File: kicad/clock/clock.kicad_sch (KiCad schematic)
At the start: 6 parts

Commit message: Working on clock
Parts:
- removed U5: ~, Package_DIP:DIP-14_W7.62mm, symbol custom_symbol_lib:quad_and
- removed U6: ~, Package_DIP:DIP-14_W7.62mm, symbol custom_symbol_lib:6xNOT
- removed U7: ~, Package_DIP:DIP-14_W7.62mm, symbol custom_symbol_lib:quad_OR
- added C1: C, Capacitor_THT:C_Disc_D5.0mm_W2.5mm_P5.00mm, symbol Device:C
- added R2, R3, R4, R5: R, custom_footprint_library:0.4_pitch_resistor, symbol Device:R
- added U4: ~, Package_DIP:DIP-14_W7.62mm, symbol custom_symbol_lib:OP_AMP_quad
- U1: footprint custom_footprint_library:bus_connector -> Connector_PinHeader_2.54mm:PinHeader_1x23_P2.54mm_Vertical
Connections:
- net at U2.7 (Q7), U3.7 (Q7): now also U1.14 (D0); no longer U1.12 (D0)
- net at U2.6 (Q6), U3.6 (Q6): now also U1.15 (D1); no longer U1.13 (D1)
- net at U2.5 (Q5), U3.5 (Q5): now also U1.16 (D2); no longer U1.14 (D2)
- net at U2.4 (Q4), U3.4 (Q4): now also U1.17 (D3); no longer U1.15 (D3)
- net at U2.3 (Q3), U3.3 (Q3): now also U1.18 (D4); no longer U1.16 (D4)
- net at U2.2 (Q2), U3.2 (Q2): now also U1.19 (D5); no longer U1.17 (D5)
- net at U2.1 (Q1), U3.1 (Q1): now also U1.20 (D6); no longer U1.18 (D6)
- net at U2.15 (Q0), U3.15 (Q0): now also U1.21 (D7); no longer U1.19 (D7)
- net at U3.11 (CCLK): now also U2.9 (RCO#); no longer U2.11 (CCLK)
- net at U3.12 (CCKEN#): now also U2.12 (CCKEN#), U2.8 (GND); no longer U2.9 (RCO#)
- new net: R2.1, U4.4 (V+)
- new net: R2.2, R3.1, R5.2, U4.3 (IN+_1)
- new net: C1.1, R4.2, U4.2 (IN-_1)
- new net: C1.2, R3.2, U4.10 (IN+_3), U4.11 (GND), U4.12 (IN+_4), U4.13 (IN-_4), U4.5 (IN+_2), U4.6 (IN-_2), U4.9 (IN-_3)
- new net: R4.1, R5.1, U4.1 (OUT_1)
- no-connect marks 4 -> 9
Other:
- note added: "Counter A"
- note added: "Counter B"
- note removed: "A & B CLK generator"
- note removed: "Auto clock source"
- note removed: "Manual / auto clock selector"

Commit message: Working on clock
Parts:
- added R1, R6, R7, R8: R, custom_footprint_library:0.4_pitch_resistor, symbol Device:R
- added U10, U14, U17, U5: ~, Package_DIP:DIP-14_W7.62mm, symbol custom_symbol_lib:quad_and
- added U11: ~, Package_DIP:DIP-14_W7.62mm, symbol custom_symbol_lib:dual_latch
- added U12, U15, U16, U18, U20, U21: ~, custom_footprint_library:jumper, symbol custom_symbol_lib:jumper
- added U13, U6: ~, Package_DIP:DIP-14_W7.62mm, symbol custom_symbol_lib:6xNOT
- added U19: ~, Package_DIP:DIP-16_W7.62mm, symbol custom_symbol_lib:8_bit_counter
- added U7, U8: ~, Connector_PinHeader_2.54mm:PinHeader_1x03_P2.54mm_Vertical, symbol custom_symbol_lib:switch_SPDT
- added U9: ~, Package_DIP:DIP-14_W7.62mm, symbol custom_symbol_lib:quad_OR
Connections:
- net at R2.1, U4.4 (V+): now also U1.12 (V+), U2.10 (CCLR#), U2.16 (V+), U3.10 (CCLR#), U3.16 (V+), R1.1, R6.1, U10.14 (V+), U11.14 (V+), U13.14 (V+), U14.14 (V+), U17.14 (V+), U19.10 (CCLR#), U19.16 (V+), U5.14 (V+), U6.14 (V+), U9.14 (V+)
- net at C1.2, R3.2, U4.10 (IN+_3)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: now also U1.13 (GND), U2.12 (CCKEN#), U2.8 (GND), U3.12 (CCKEN#), U3.8 (GND), U10.7 (GND), U11.10 (1RESET), U11.4 (0RESET), U11.6 (0SET), U11.7 (GND), U11.8 (1SET), U12.2 (GND), U13.7 (GND), U14.7 (GND), U15.2 (GND), U16.2 (GND), U17.12 (3B), U17.13 (3A), U17.4 (2A), U17.5 (2B), U17.7 (GND), U18.2 (GND), U19.12 (CCKEN#), U19.14 (OE#), U19.8 (GND), U20.2 (GND), U21.2 (GND), U5.7 (GND), U6.13 (I5), U6.7 (GND), U7.2 (2_(middle)), U8.2 (2_(middle)), U9.5 (1A), U9.6 (1B), U9.7 (GND)
- net at R4.1, R5.1, U4.1 (OUT_1): now also U12.1 (IN)
- net at U1.10 (CLK_A): now also U21.3 (OUT)
- net at U1.11 (CLK_B): now also U11.11 (1CLK), U11.3 (0CLK), U20.3 (OUT)
- net at U1.22 (FAULT): now also U17.2 (1B)
- net at U1.23 (ENABLE): now also U10.10 (4A), U10.12 (3B)
- net at U1.5 (WRITE_0): now also U10.1 (1A)
- net at U1.6 (WRITE_1): now also U10.4 (2A)
- net at U1.9 (READ_READY): now also U9.11 (Q3)
- net at U3.13 (RCLK): now also U10.8 (4Q), U13.5 (I2), U9.13 (3B)
- net at U3.14 (OE#): now also U13.6 (O2)
- net at U2.11 (CCLK): now also U18.3 (OUT), U19.11 (CCLK), U19.13 (RCLK)
- net at U2.13 (RCLK): now also U10.11 (3Q), U13.9 (I3), U9.12 (3A)
- net at U2.14 (OE#): now also U13.8 (03)
- new net: R1.2, U5.1 (1A), U7.1
- new net: R6.2, U5.4 (2A), U7.3
- new net: U17.9 (4B), U19.1 (Q1), U9.9 (2B)
- new net: U13.11 (I4), U19.15 (Q0), U9.8 (2A)
- new net: U12.3 (OUT), U14.12 (3B)
- new net: U20.1 (IN), U6.10 (O4)
- new net: U16.1 (IN), U5.5 (2B), U6.4 (O1)
- new net: U14.9 (4B), U16.3 (OUT)
- new net: U14.11 (3Q), U9.1 (0A)
- new net: U6.11 (I4), U9.10 (Q2)
- new net: U14.8 (4Q), U9.2 (0B)
- new net: U18.1 (IN), U9.3 (Q0)
- new net: U10.13 (3A), U11.1 (0Q)
- new net: U10.5 (2B), U11.12 (1Q3)
- new net: U10.9 (4B), U11.13 (1Q)
- new net: U10.2 (1B), U11.2 (0Q#)
- new net: U10.3 (1Q), U11.5 (0D)
- new net: U10.6 (2Q), U11.9 (1D)
- new net: U14.2 (1B), U15.3 (OUT), U17.1 (1A)
- new net: U13.10 (O4), U17.10 (4A)
- new net: U13.13 (I5), U17.3 (1Q)
- new net: U17.8 (4Q), U21.1 (IN)
- new net: R7.1, R8.1
- new net: R7.2, U5.13 (3A), U8.1
- new net: U13.4 (O1), U14.1 (1A), U14.10 (4A)
- new net: U13.2 (O0), U14.13 (3A), U14.5 (2B)
- new net: U13.1 (I0), U14.3 (1Q)
- new net: U13.12 (O5), U14.4 (2A)
- new net: U13.3 (I1), U14.6 (2Q)
- new net: U15.1 (IN), U5.12 (3B), U6.6 (O2)
- new net: R8.2, U5.10 (4A), U8.3
- new net: U5.6 (2Q), U6.1 (I0)
- new net: U5.2 (1B), U6.2 (O0)
- new net: U5.3 (1Q), U6.3 (I1)
- new net: U5.8 (4Q), U6.5 (I2)
- new net: U5.9 (4B), U6.8 (03)
- new net: U5.11 (3Q), U6.9 (I3)
- no-connect marks 9 -> 21
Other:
- note added: "A CLK"
- note added: "Auto clock source"
- note added: "B CLK"
- note added: "Clock"
- note added: "Fault enable"
- note added: "Fault override"
- note added: "Fault override & manual clock debouncers"
- note added: "Manual clock"
- note added: "WRITE 1: CLK-COUNTER-B WRITE 0: CLK-COUNTER-A"
- note removed: "Counter & selector"
- note removed: "WRITE 1: CLK-B WRITE 0: CLK-A"
- moved on the sheet: C1, R2, R3, R4, R5, U1, U2, U3, U4

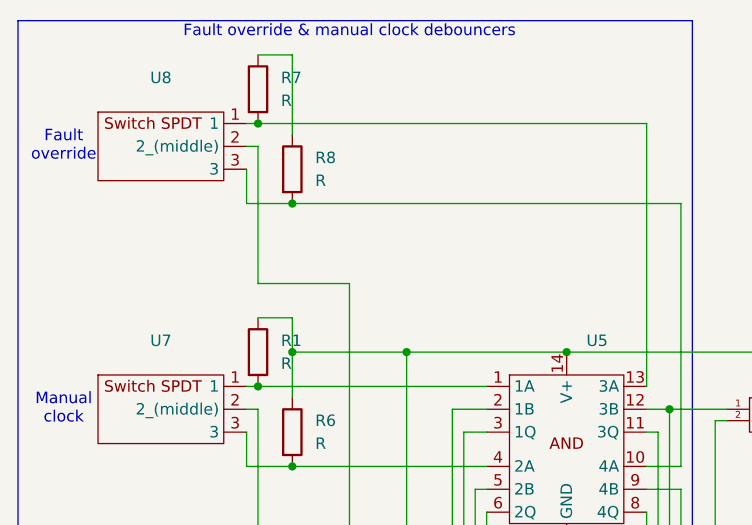
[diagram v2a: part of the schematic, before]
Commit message: Increased clock PCB clearances
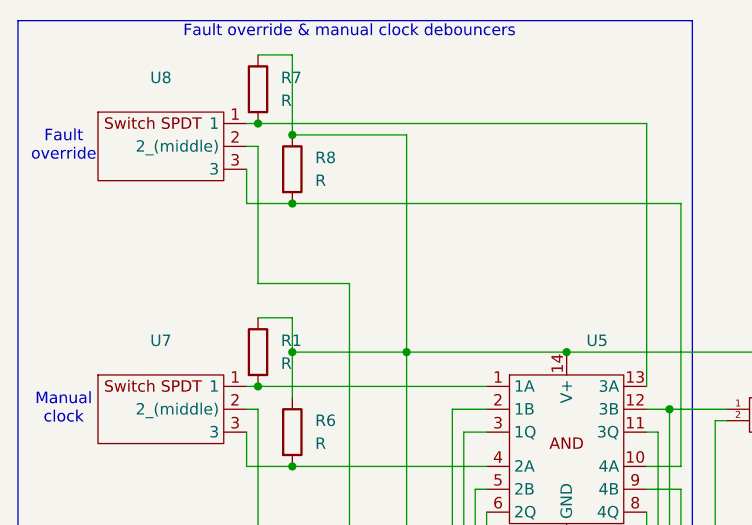
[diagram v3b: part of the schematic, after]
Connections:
- net at R1.1, R2.1, R6.1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: now also R7.1, R8.1
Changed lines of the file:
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@@
+	)
+	(junction
+		(at 49.53 29.21)
+		(diameter 0)
+		(color 0 0 0 0)
 	)
 	(junction
@@
 	(wire
 		(pts
+			(xy 62.23 29.21) (xy 62.23 53.34)
+		)
+		(stroke
+			(width 0)
+			(type default)
+		)
+	)
+	(wire
+		(pts
 			(xy 158.75 50.8) (xy 158.75 44.45)
 		)
@@
 		)
 		(stroke
+			(width 0)
+			(type default)
+		)
+	)
+	(wire
+		(pts
+			(xy 49.53 29.21) (xy 62.23 29.21)
+		)
+		(stroke

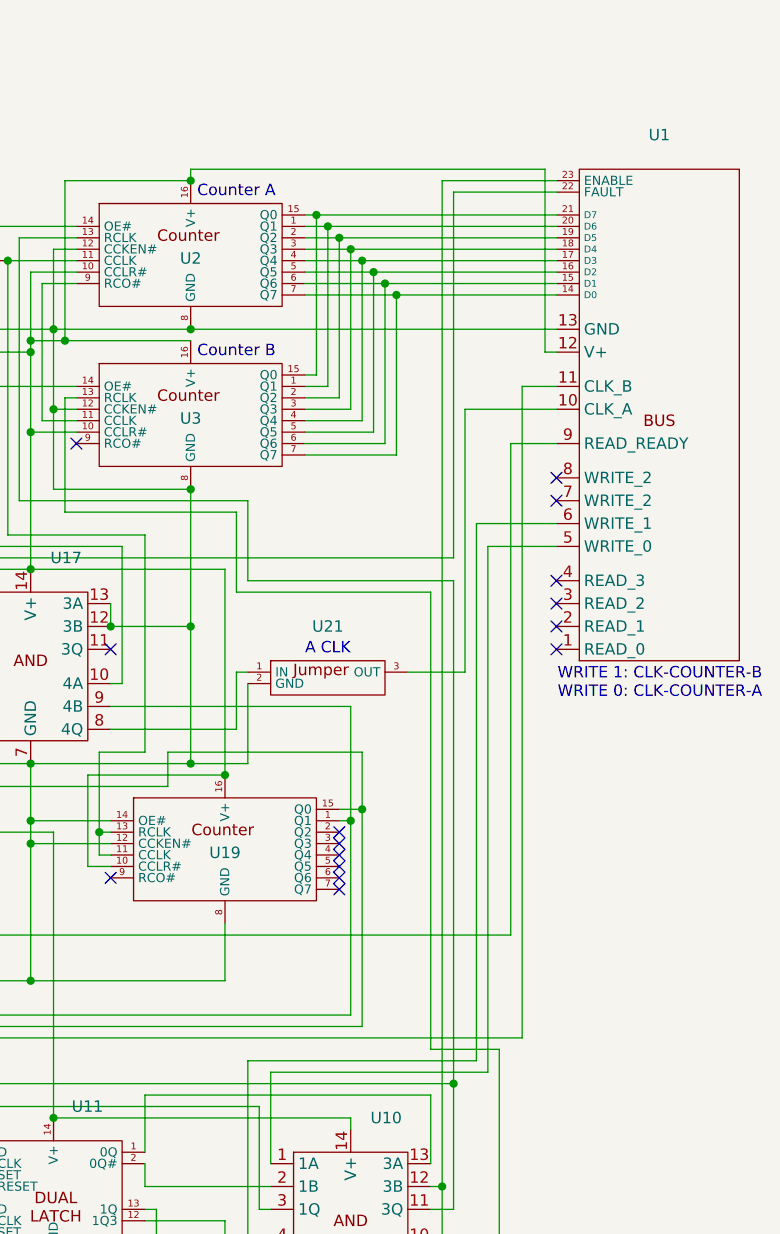
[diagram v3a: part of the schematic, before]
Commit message: Added pulldown resistors to clock module inputs
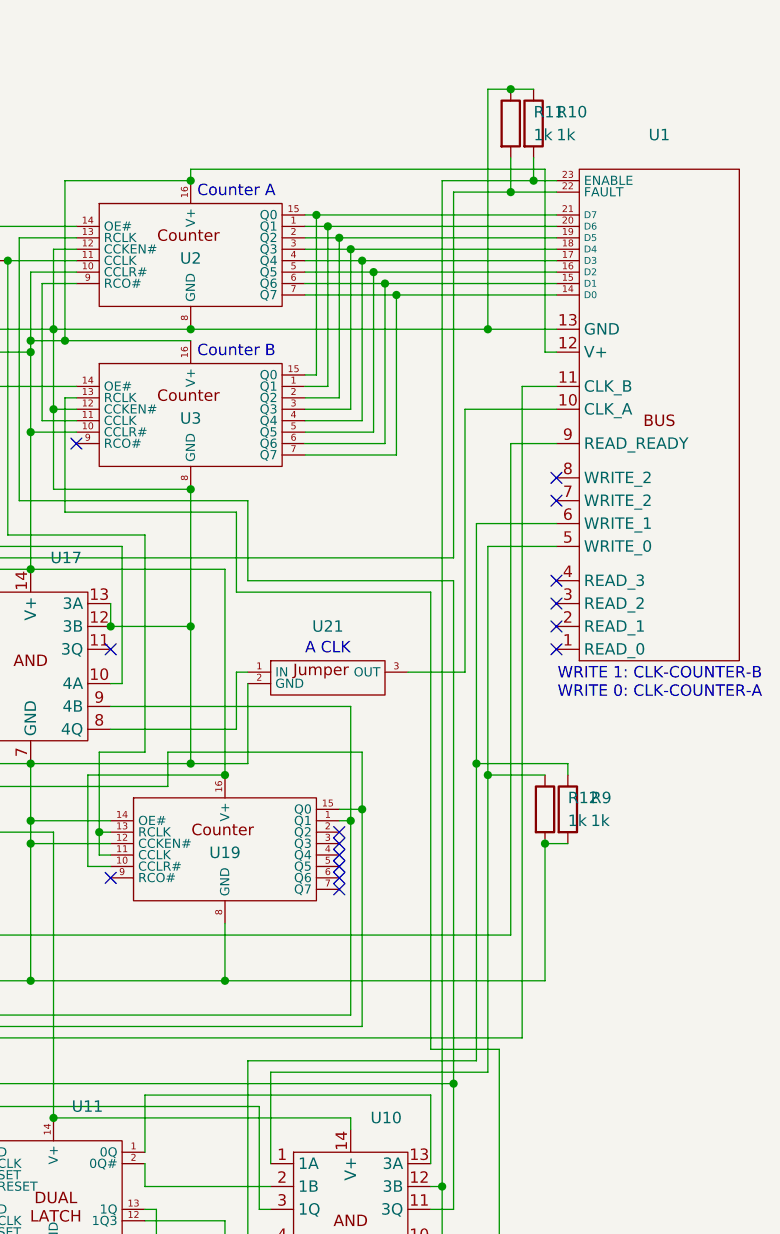
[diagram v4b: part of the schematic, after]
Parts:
- added R10, R11, R12, R9: 1k, custom_footprint_library:0.4_pitch_resistor, symbol Device:R
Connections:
- net at C1.2, R3.2, U1.13 (GND)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: now also R10.1, R11.1, R12.2, R9.2
- net at U1.22 (FAULT), U17.2 (1B): now also R11.2
- net at U1.23 (ENABLE), U10.10 (4A), U10.12 (3B): now also R10.2
- net at U1.5 (WRITE_0), U10.1 (1A): now also R12.1
- net at U1.6 (WRITE_1), U10.4 (2A): now also R9.1

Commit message: Finished IO controller schematic
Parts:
- C1: footprint Capacitor_THT:C_Disc_D5.0mm_W2.5mm_P5.00mm -> Capacitor_THT:CP_Radial_Tantal_D5.0mm_P5.00mm
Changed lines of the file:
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@@
 			)
 		)
-		(property "Footprint" "Capacitor_THT:C_Disc_D5.0mm_W2.5mm_P5.00mm"
+		(property "Footprint" "Capacitor_THT:CP_Radial_Tantal_D5.0mm_P5.00mm"
 			(at 40.3352 130.81 0)
 			(effects
